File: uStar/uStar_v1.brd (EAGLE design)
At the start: 85 x 40 mm, 38 parts, among them IC1 INA138, X1 BU-SMA-V

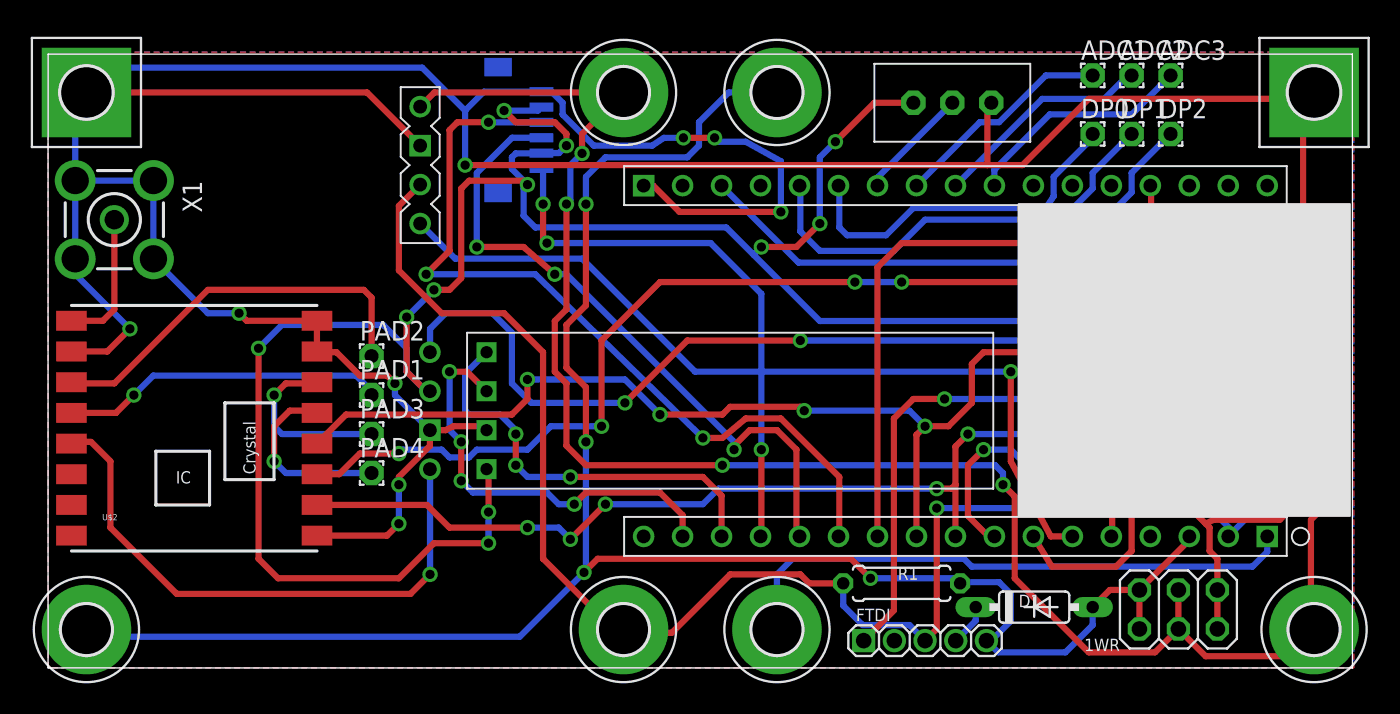
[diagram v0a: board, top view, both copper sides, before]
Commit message: added ADC lines instead of the uneeded ground
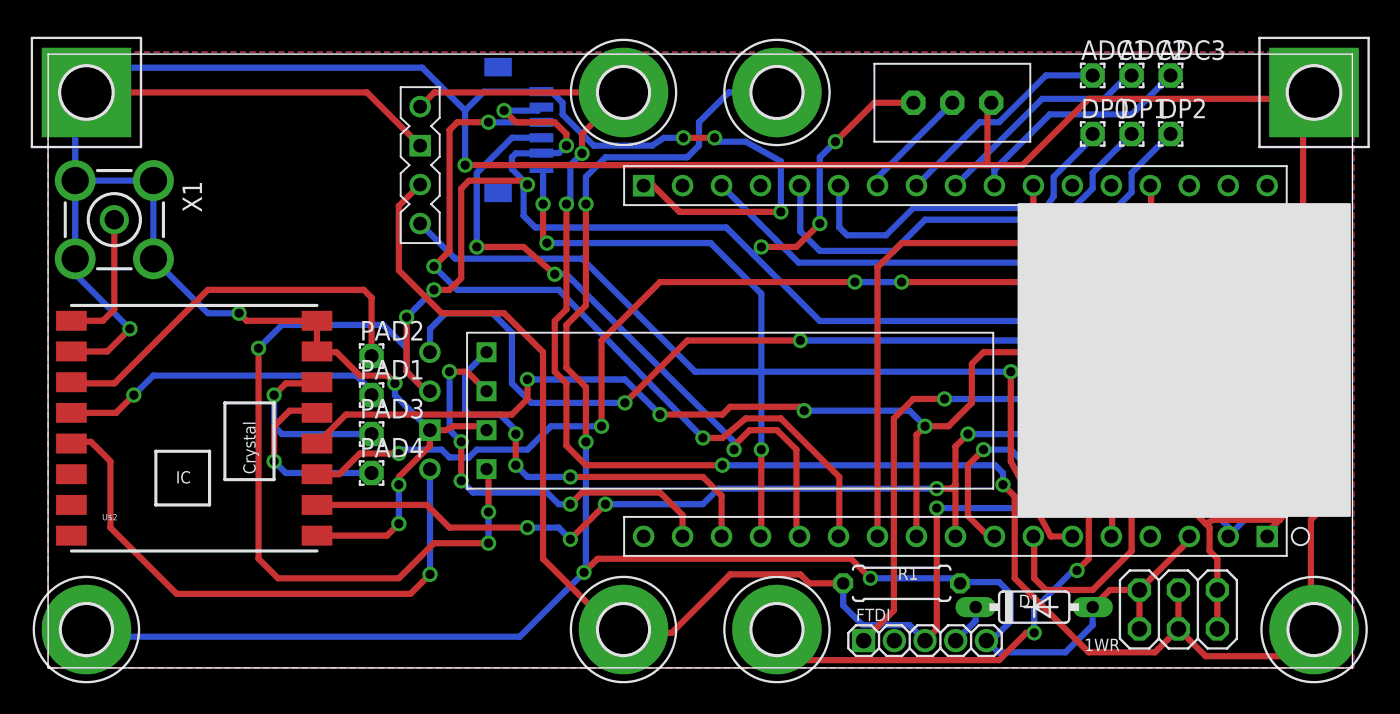
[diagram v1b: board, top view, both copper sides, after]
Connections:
- removed net EXT_GND: EXT-GND.B3,3, U$1.GND
- new net BATT_LEVEL: EXT-GND.B3,3, U$1.P24
- net GND: now also U$1.GND
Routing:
- net BATT_LEVEL: track 0.00 -> 53.0 mm, vias 0 -> 4
- net EXT_GND: track 37.6 -> 0.00 mm
- net RADIO_SHDN: track 74.6 -> 77.1 mm
- net GND: track 311.6 -> 313.0 mm
- net GPS_TX: track 53.4 -> 52.6 mm
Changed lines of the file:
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@@
 <wire x1="80.264" y1="9.652" x2="80.96" y2="10.348" width="0.4064" layer="1"/>
 <wire x1="80.96" y1="10.348" x2="80.96" y2="12.7" width="0.4064" layer="1"/>
+<contactref element="U$1" pad="GND"/>
+<wire x1="79.45" y1="8.57" x2="79.45" y2="8.838" width="0.4064" layer="1"/>
+<wire x1="79.45" y1="8.838" x2="80.264" y2="9.652" width="0.4064" layer="1"/>
 </signal>
 <signal name="+3V3">
@@
 <wire x1="75.228" y1="15.45" x2="77.26" y2="15.45" width="0.4064" layer="1"/>
 <wire x1="56.388" y1="36.83" x2="53.848" y2="36.83" width="0.4064" layer="1"/>
-<wire x1="53.848" y1="36.83" x2="51.308" y2="34.29" width="0.4064" layer="1"/>
-<via x="51.308" y="34.29" extent="1-16" drill="0.6" shape="square"/>
-<wire x1="51.308" y1="34.29" x2="50.292" y2="33.274" width="0.4064" layer="16"/>
 <wire x1="50.292" y1="33.274" x2="50.292" y2="28.956" width="0.4064" layer="16"/>
 <via x="50.292" y="28.956" extent="1-16" drill="0.6"/>
@@
 <via x="46.482" y="27.432" extent="1-16" drill="0.6"/>
 <wire x1="46.482" y1="27.432" x2="45.974" y2="26.924" width="0.4064" layer="16"/>
+<wire x1="53.848" y1="36.83" x2="51.308" y2="34.29" width="0.4064" layer="1"/>
+<via x="51.308" y="34.29" extent="1-16" drill="0.6"/>
+<wire x1="51.308" y1="34.29" x2="50.292" y2="33.274" width="0.4064" layer="16"/>
 </signal>
 <signal name="1WIRE">
@@
 <contactref element="U$3" pad="SHDN"/>
 <contactref element="U$1" pad="P7"/>
-<wire x1="64.21" y1="8.57" x2="65.414" y2="6.604" width="0.4064" layer="1"/>
-<wire x1="65.414" y1="6.604" x2="69.596" y2="6.604" width="0.4064" layer="1"/>
-<wire x1="69.596" y1="6.604" x2="70.612" y2="7.62" width="0.4064" layer="1"/>
 <wire x1="70.612" y1="7.62" x2="70.612" y2="16.51" width="0.4064" layer="1"/>
 <via x="70.612" y="16.51" extent="1-16" drill="0.6"/>
@@
 <wire x1="24.892" y1="20.583" x2="24.883" y2="20.574" width="0.4064" layer="16"/>
 <wire x1="37.592" y1="17.272" x2="41.656" y2="21.336" width="0.4064" layer="1"/>
+<wire x1="70.612" y1="7.62" x2="68.072" y2="5.08" width="0.4064" layer="1"/>
+<wire x1="68.072" y1="5.08" x2="65.024" y2="5.08" width="0.4064" layer="1"/>
+<wire x1="65.024" y1="5.08" x2="64.262" y2="5.842" width="0.4064" layer="1"/>
+<wire x1="64.262" y1="5.842" x2="64.262" y2="8.518" width="0.4064" layer="1"/>
+<wire x1="64.262" y1="8.518" x2="64.21" y2="8.57" width="0.4064" layer="1"/>
 </signal>
 <signal name="GPS_SHDN">
@@
 <wire x1="41.35" y1="8.57" x2="41.35" y2="9.958" width="0.4064" layer="1"/>
 <wire x1="41.35" y1="9.958" x2="39.878" y2="11.43" width="0.4064" layer="1"/>
-<wire x1="39.878" y1="11.43" x2="35.052" y2="11.43" width="0.4064" layer="1"/>
-<wire x1="35.052" y1="11.43" x2="34.29" y2="10.668" width="0.4064" layer="1"/>
-<via x="34.29" y="10.668" extent="1-16" drill="0.6"/>
-<wire x1="34.29" y1="10.668" x2="33.274" y2="10.668" width="0.4064" layer="16"/>
+<via x="34.036" y="10.668" extent="1-16" drill="0.6"/>
+<wire x1="34.036" y1="10.668" x2="33.274" y2="10.668" width="0.4064" layer="16"/>
 <wire x1="33.274" y1="10.668" x2="32.512" y2="11.43" width="0.4064" layer="16"/>
 <wire x1="32.512" y1="11.43" x2="27.686" y2="11.43" width="0.4064" layer="16"/>
@@
 <wire x1="27.305" y1="19.304" x2="28.575" y2="18.034" width="0.4064" layer="1"/>
 <wire x1="26.162" y1="15.494" x2="26.924" y2="14.732" width="0.4064" layer="16"/>
+<wire x1="34.036" y1="10.668" x2="34.798" y2="11.43" width="0.4064" layer="1"/>
+<wire x1="34.798" y1="11.43" x2="39.878" y2="11.43" width="0.4064" layer="1"/>
 </signal>
 <signal name="9DOF_SDA">
@@
 <wire x1="26.67" y1="35.56" x2="26.162" y2="35.052" width="0.4064" layer="1"/>
 <wire x1="26.162" y1="35.052" x2="26.162" y2="27.178" width="0.4064" layer="1"/>
-<wire x1="26.162" y1="27.178" x2="24.638" y2="25.654" width="0.4064" layer="1"/>
-<via x="24.638" y="25.654" extent="1-16" drill="0.6"/>
 <via x="42.672" y="14.986" extent="1-16" drill="0.6"/>
 <wire x1="42.672" y1="14.986" x2="43.942" y2="14.986" width="0.4064" layer="1"/>
@@
 <wire x1="51.562" y1="12.446" x2="51.562" y2="8.622" width="0.4064" layer="1"/>
 <wire x1="51.562" y1="8.622" x2="51.51" y2="8.57" width="0.4064" layer="1"/>
-<wire x1="24.638" y1="25.654" x2="31.75" y2="25.654" width="0.4064" layer="16"/>
-<wire x1="31.75" y1="25.654" x2="42.672" y2="14.986" width="0.4064" layer="16"/>
+<wire x1="33.274" y1="24.638" x2="42.672" y2="14.986" width="0.4064" layer="16"/>
+<wire x1="26.162" y1="27.178" x2="25.146" y2="26.162" width="0.4064" layer="1"/>
+<via x="25.146" y="26.162" extent="1-16" drill="0.6"/>
+<wire x1="25.146" y1="26.162" x2="26.67" y2="24.638" width="0.4064" layer="16"/>
+<wire x1="26.67" y1="24.638" x2="33.274" y2="24.638" width="0.4064" layer="16"/>
 </signal>
 <signal name="SD_SELECT">
@@
 <wire x1="48.904" y1="26.416" x2="43.89" y2="31.43" width="0.4064" layer="16"/>
 </signal>
-<signal name="EXT_GND">
+<signal name="BATT_LEVEL">
 <contactref element="EXT-GND" pad="B3,3"/>
-<contactref element="U$1" pad="GND"/>
-<wire x1="79.45" y1="8.57" x2="79.45" y2="7.568" width="0.4064" layer="16"/>
-<wire x1="79.45" y1="7.568" x2="78.486" y2="6.604" width="0.4064" layer="16"/>
-<wire x1="78.486" y1="6.604" x2="60.198" y2="6.604" width="0.4064" layer="16"/>
-<wire x1="60.198" y1="6.604" x2="59.69" y2="7.112" width="0.4064" layer="16"/>
-<wire x1="59.69" y1="7.112" x2="48.514" y2="7.112" width="0.4064" layer="16"/>
-<wire x1="48.514" y1="7.112" x2="47.498" y2="6.096" width="0.4064" layer="16"/>
-<wire x1="47.498" y1="6.096" x2="47.498" y2="2.502" width="0.4064" layer="16"/>
-<wire x1="47.498" y1="2.502" x2="47.5" y2="2.5" width="0.4064" layer="16"/>
+<contactref element="U$1" pad="P24"/>
+<wire x1="64.21" y1="31.43" x2="64.21" y2="30.024" width="0.4064" layer="1"/>
+<wire x1="64.21" y1="30.024" x2="65.278" y2="28.956" width="0.4064" layer="1"/>
+<wire x1="65.278" y1="28.956" x2="67.31" y2="28.956" width="0.4064" layer="1"/>
+<wire x1="67.31" y1="28.956" x2="69.342" y2="26.924" width="0.4064" layer="1"/>
+<wire x1="69.342" y1="26.924" x2="69.342" y2="20.828" width="0.4064" layer="1"/>
+<wire x1="69.342" y1="20.828" x2="67.818" y2="19.304" width="0.4064" layer="1"/>
+<via x="67.818" y="19.304" extent="1-16" drill="0.6"/>
+<wire x1="67.818" y1="19.304" x2="67.818" y2="12.192" width="0.4064" layer="16"/>
+<via x="67.818" y="12.192" extent="1-16" drill="0.6"/>
+<wire x1="67.818" y1="12.192" x2="67.818" y2="7.112" width="0.4064" layer="1"/>
+<wire x1="67.818" y1="7.112" x2="67.056" y2="6.35" width="0.4064" layer="1"/>
+<via x="67.056" y="6.35" extent="1-16" drill="0.6"/>
+<wire x1="67.056" y1="6.35" x2="66.802" y2="6.35" width="0.4064" layer="16"/>
+<wire x1="66.802" y1="6.35" x2="64.262" y2="3.81" width="0.4064" layer="16"/>
+<wire x1="64.262" y1="3.81" x2="64.262" y2="2.286" width="0.4064" layer="16"/>
+<via x="64.262" y="2.286" extent="1-16" drill="0.6"/>
+<wire x1="64.262" y1="2.286" x2="63.754" y2="2.286" width="0.4064" layer="1"/>
+<wire x1="63.754" y1="2.286" x2="61.976" y2="0.508" width="0.4064" layer="1"/>
+<wire x1="61.976" y1="0.508" x2="49.492" y2="0.508" width="0.4064" layer="1"/>
+<wire x1="49.492" y1="0.508" x2="47.5" y2="2.5" width="0.4064" layer="1"/>
 </signal>
 </signals>

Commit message: fixed clearance violations
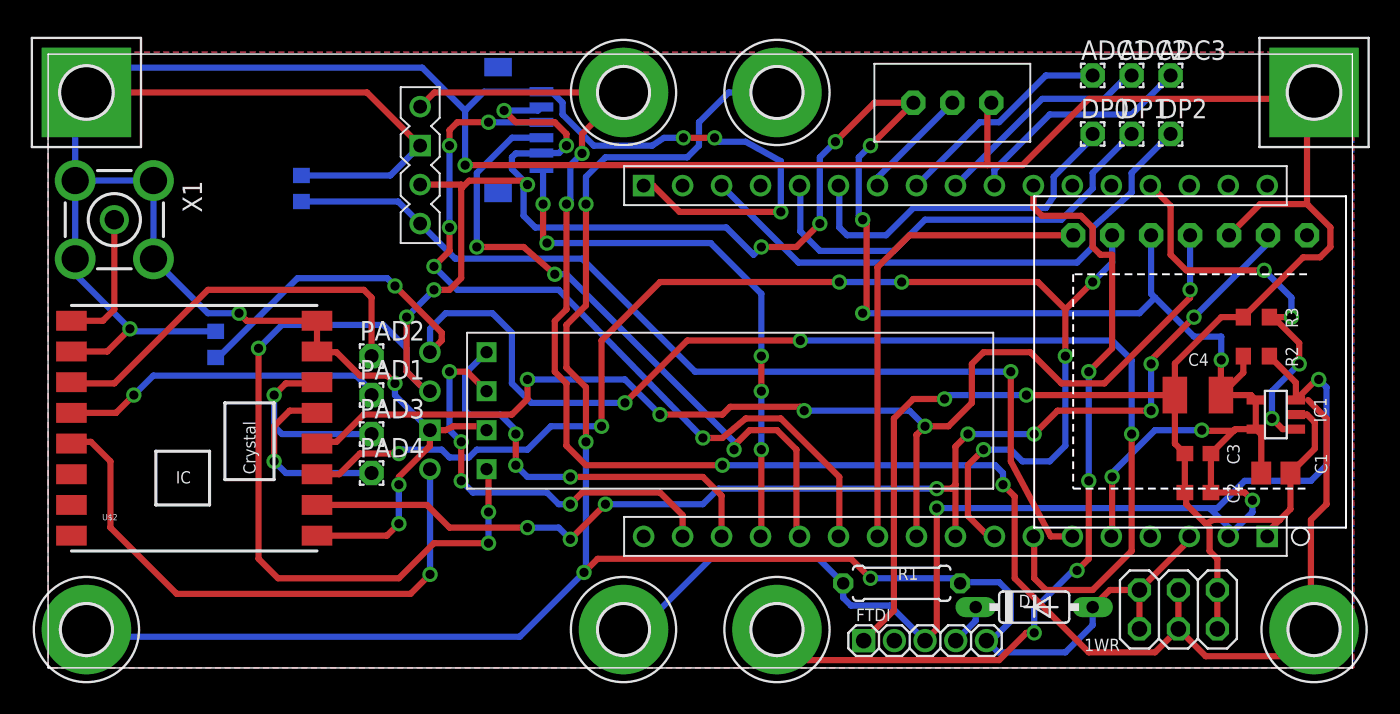
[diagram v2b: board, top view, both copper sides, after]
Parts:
- added R4, R5: 50K, rcl:R0603
- U$6: value BOB-00544 -> SDCARD_EXT; device LearningByMaking:BOB-00544 -> LearningByMaking:SDCARD_EXT
- moved U$6 14.0 mm to (74.4, 19.3), flipped to the bottom
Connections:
- net +3V3: now also U$7.VIN
- net EXT_VCC: no longer U$7.VIN
- net GND: now also R4.1, R5.1
- net RADIO_SHDN: now also R5.2
- net RAIL_SHDN: now also R4.2
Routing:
- net EXT_VCC: track 111.9 -> 73.5 mm
- net GND: track 313.0 -> 335.7 mm, vias 10 -> 11
- net MISO: track 55.7 -> 78.2 mm, vias 5 -> 9
- net RADIO_SHDN: track 77.1 -> 97.1 mm, vias 3 -> 4
- net CLK: track 62.3 -> 79.2 mm, vias 4 -> 5
- net +3V3: track 193.1 -> 206.5 mm, vias 15 -> 18
- net RAIL_SHDN: track 55.3 -> 63.6 mm
- net MOSI: track 80.4 -> 86.5 mm, vias 6 -> 7
- net SD_SELECT: track 28.7 -> 31.2 mm
- net BATT_LEVEL: track 53.0 -> 53.8 mm
- net N$13: track 35.6 -> 36.2 mm
- net GPS_TX: vias 3 -> 5
- net GPS_SHDN: vias 3 -> 5

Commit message: refined and executed the DRC process, made appropriate changes
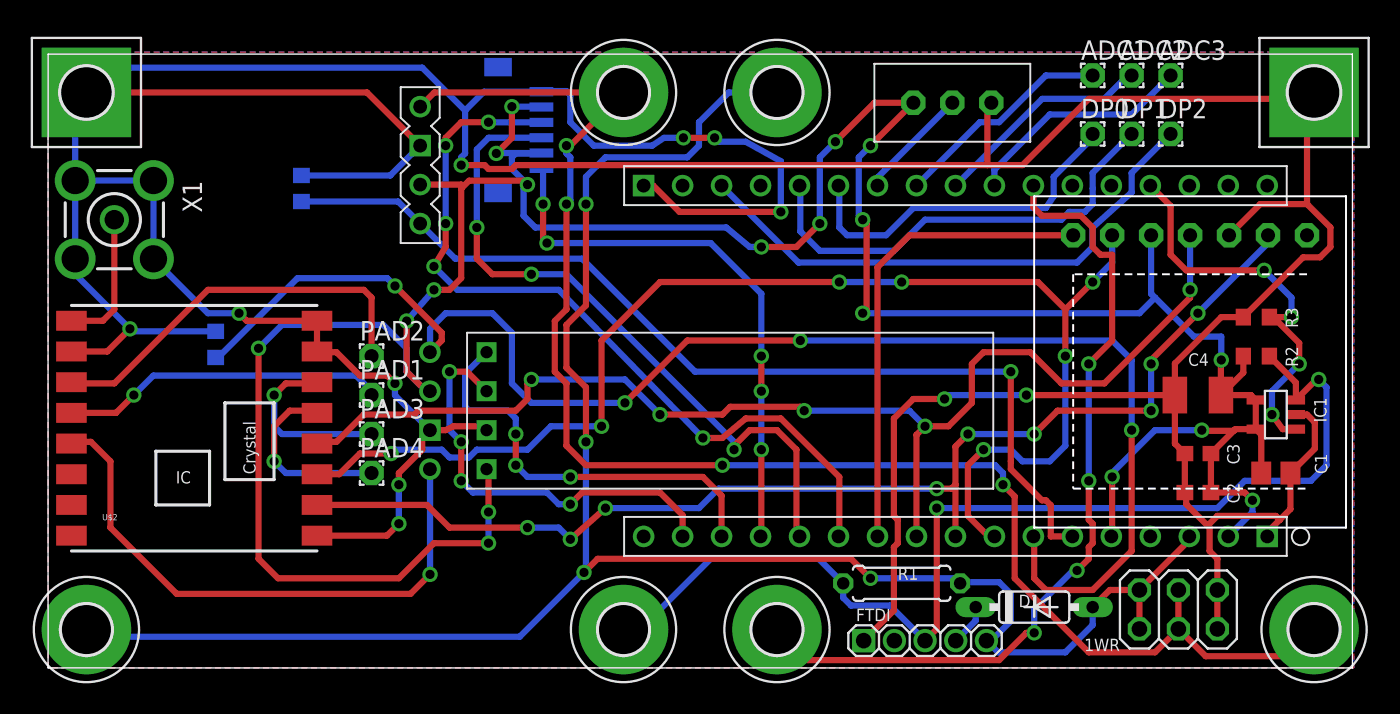
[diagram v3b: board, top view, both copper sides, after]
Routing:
- net VCC: track 117.3 -> 101.7 mm
- net EXT_VCC: track 73.5 -> 71.2 mm
- net +3V3: track 206.5 -> 204.5 mm
- net GND: track 335.7 -> 337.3 mm
- net GPS_RX: track 43.5 -> 44.9 mm
- net N$12: track 28.9 -> 29.5 mm
- net RAIL_SHDN: track 63.6 -> 64.2 mm
- net 9DOF_SDA: track 27.4 -> 27.9 mm
